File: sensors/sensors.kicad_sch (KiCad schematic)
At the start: 5 parts, among them J1 GPIO, J3 JP_PWM, J4 JP_ADC

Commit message: move buzzer to power board
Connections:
- no-connect marks 14 -> 15
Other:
- removed sheet Buzzer
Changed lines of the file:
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@@
 	)
 	(no_connect
+		(at 73.66 74.93)
+	)
+	(no_connect
 		(at 60.96 82.55)
 	)
@@
 	(wire
 		(pts
-			(xy 294.64 189.23) (xy 297.18 189.23)
-		)
-		(stroke
-			(width 0)
-			(type default)
-		)
-	)
-	(wire
-		(pts
 			(xy 54.61 214.63) (xy 54.61 212.09)
 		)
@@
 		)
 	)
-	(label "GPIO12{slash}PWM0"
-		(at 297.18 189.23 0)
-		(effects
-			(font
-				(size 1.27 1.27)
-			)
-			(justify left bottom)
-		)
-	)
 	(label "GPIO17"
 		(at 31.75 49.53 0)
@@
 				)
 			)
-		)
-	)
-	(sheet
-		(at 266.7 180.34)
-		(size 27.94 17.78)
-		(exclude_from_sim no)
-		(in_bom yes)
-		(on_board yes)
-		(dnp no)
-		(fields_autoplaced yes)
-		(stroke
-			(width 0.1524)
-			(type solid)
-		)
-		(fill
-			(color 0 0 0 0)
-		)
-		(property "Sheetname" "Buzzer"
-			(at 266.7 179.6284 0)
-			(show_name no)
-			(do_not_autoplace no)
-			(effects
-				(font
-					(size 1.27 1.27)
-				)
-				(justify left bottom)
-			)
-		)
-		(property "Sheetfile" "_buzzer.kicad_sch"
-			(at 266.7 198.7046 0)
-			(show_name no)
-			(do_not_autoplace no)
-			(effects
-				(font
-					(size 1.27 1.27)
-				)
-				(justify left top)
-			)
-		)
-		(pin "PWM" input
-			(at 294.64 189.23 0)
-			(effects
-				(font
-					(size 1.27 1.27)
-				)
-				(justify right)
-			)
-		)
-		(instances
-			(project "sensors"
-				(path "/e63e39d7-6ac0-4ffd-8aa3-1841a4541b55"
-					(page "10")
-				)
-			)

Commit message: add Vref
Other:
- added sheet Vref (_vref.kicad_sch)
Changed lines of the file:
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@@
+	)
+	(sheet
+		(at 62.23 239.395)
+		(size 27.94 17.145)
+		(exclude_from_sim no)
+		(in_bom yes)
+		(on_board yes)
+		(dnp no)
+		(fields_autoplaced yes)
+		(stroke
+			(width 0.1524)
+			(type solid)
+		)
+		(fill
+			(color 0 0 0 0)
+		)
+		(property "Sheetname" "Vref"
+			(at 62.23 238.6834 0)
+			(show_name no)
+			(do_not_autoplace no)
+			(effects
+				(font
+					(size 1.27 1.27)
+				)
+				(justify left bottom)
+			)
+		)
+		(property "Sheetfile" "_vref.kicad_sch"
+			(at 62.23 257.1246 0)
+			(show_name no)
+			(do_not_autoplace no)
+			(effects
+				(font
+					(size 1.27 1.27)
+				)
+				(justify left top)
+			)
+		)
+		(instances
+			(project "sensors"
+				(path "/e63e39d7-6ac0-4ffd-8aa3-1841a4541b55"
+					(page "10")
+				)
+			)
+		)
 	)
 	(sheet

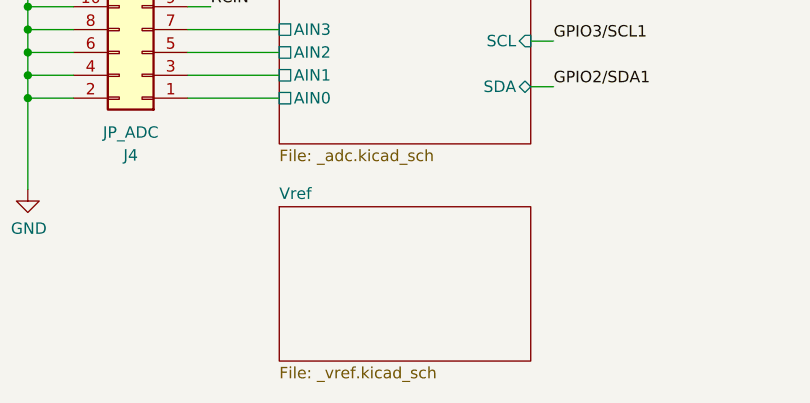
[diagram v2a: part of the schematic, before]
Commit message: remove Vref
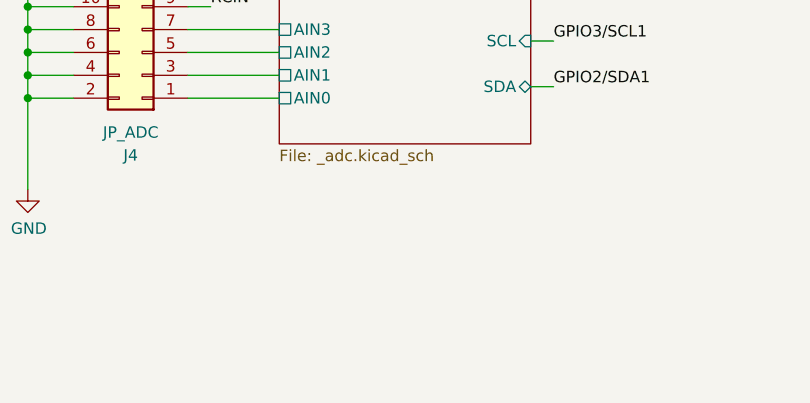
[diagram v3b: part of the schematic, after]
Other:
- removed sheet Vref
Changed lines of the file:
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@@
-	)
-	(sheet
-		(at 62.23 239.395)
-		(size 27.94 17.145)
-		(exclude_from_sim no)
-		(in_bom yes)
-		(on_board yes)
-		(dnp no)
-		(fields_autoplaced yes)
-		(stroke
-			(width 0.1524)
-			(type solid)
-		)
-		(fill
-			(color 0 0 0 0)
-		)
-		(property "Sheetname" "Vref"
-			(at 62.23 238.6834 0)
-			(show_name no)
-			(do_not_autoplace no)
-			(effects
-				(font
-					(size 1.27 1.27)
-				)
-				(justify left bottom)
-			)
-		)
-		(property "Sheetfile" "_vref.kicad_sch"
-			(at 62.23 257.1246 0)
-			(show_name no)
-			(do_not_autoplace no)
-			(effects
-				(font
-					(size 1.27 1.27)
-				)
-				(justify left top)
-			)
-		)
-		(instances
-			(project "sensors"
-				(path "/e63e39d7-6ac0-4ffd-8aa3-1841a4541b55"
-					(page "10")
-				)
-			)
-		)
 	)
 	(sheet

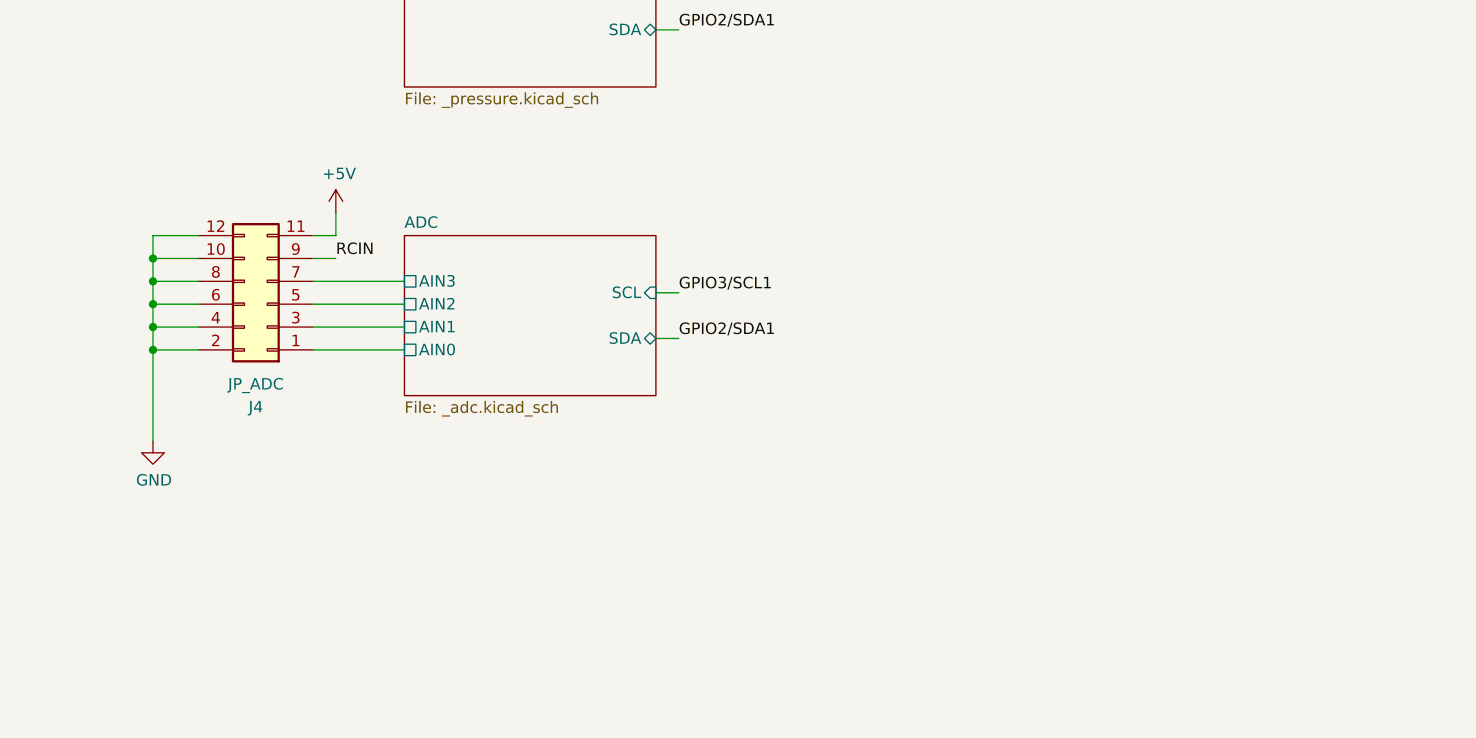
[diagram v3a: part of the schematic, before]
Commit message: added JP_VOLTS, Vref select jumper; VBAT_ADC Jumper
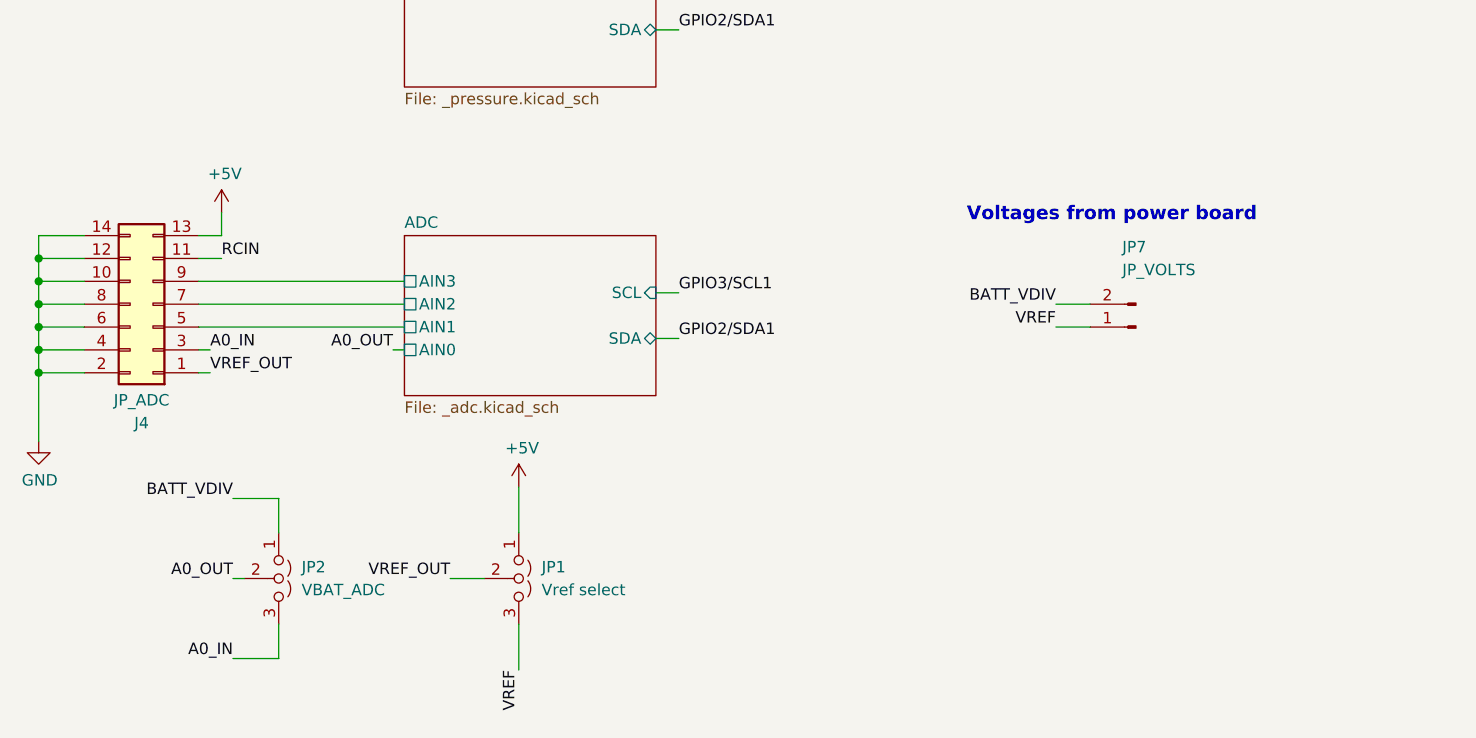
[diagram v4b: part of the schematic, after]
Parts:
- added JP1: Vref select, Connector_PinHeader_2.54mm:PinHeader_1x03_P2.54mm_Vertical, symbol Jumper:Jumper_3_Open
- added JP2: VBAT_ADC, Connector_PinHeader_2.54mm:PinHeader_1x03_P2.54mm_Vertical, symbol Jumper:Jumper_3_Open
- added JP7: JP_VOLTS, Connector_PinHeader_2.54mm:PinHeader_1x02_P2.54mm_Vertical, symbol Connector:Conn_01x02_Pin
- J4: footprint Connector_PinHeader_2.54mm:PinHeader_2x06_P2.54mm_Horizontal -> Connector_PinHeader_2.54mm:PinHeader_2x07_P2.54mm_Horizontal; symbol Connector_Generic:Conn_02x06_Odd_Even -> Connector_Generic:Conn_02x07_Odd_Even
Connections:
- net +5V: now also J4.13 (Pin_13), JP1.1 (A); no longer J4.11 (Pin_11)
- net ADC/AIN1: now also J4.5 (Pin_5); no longer J4.3 (Pin_3)
- net ADC/AIN2: now also J4.7 (Pin_7); no longer J4.5 (Pin_5)
- net ADC/AIN3: now also J4.9 (Pin_9); no longer J4.7 (Pin_7)
- net GND: now also J4.14 (Pin_14)
- net RCIN: now also J4.11 (Pin_11); no longer J4.9 (Pin_9)
- net ADC/AIN0 renamed VREF_OUT
- net VREF_OUT: now also JP1.2 (C)
- new net A0_IN: J4.3 (Pin_3), JP2.3 (B)
- new net A0_OUT: JP2.2 (C)
- new net BATT_VDIV: JP2.1 (A), JP7.2 (Pin_2)
- new net VREF: JP1.3 (B), JP7.1 (Pin_1)
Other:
- note added: "Voltages from power board"

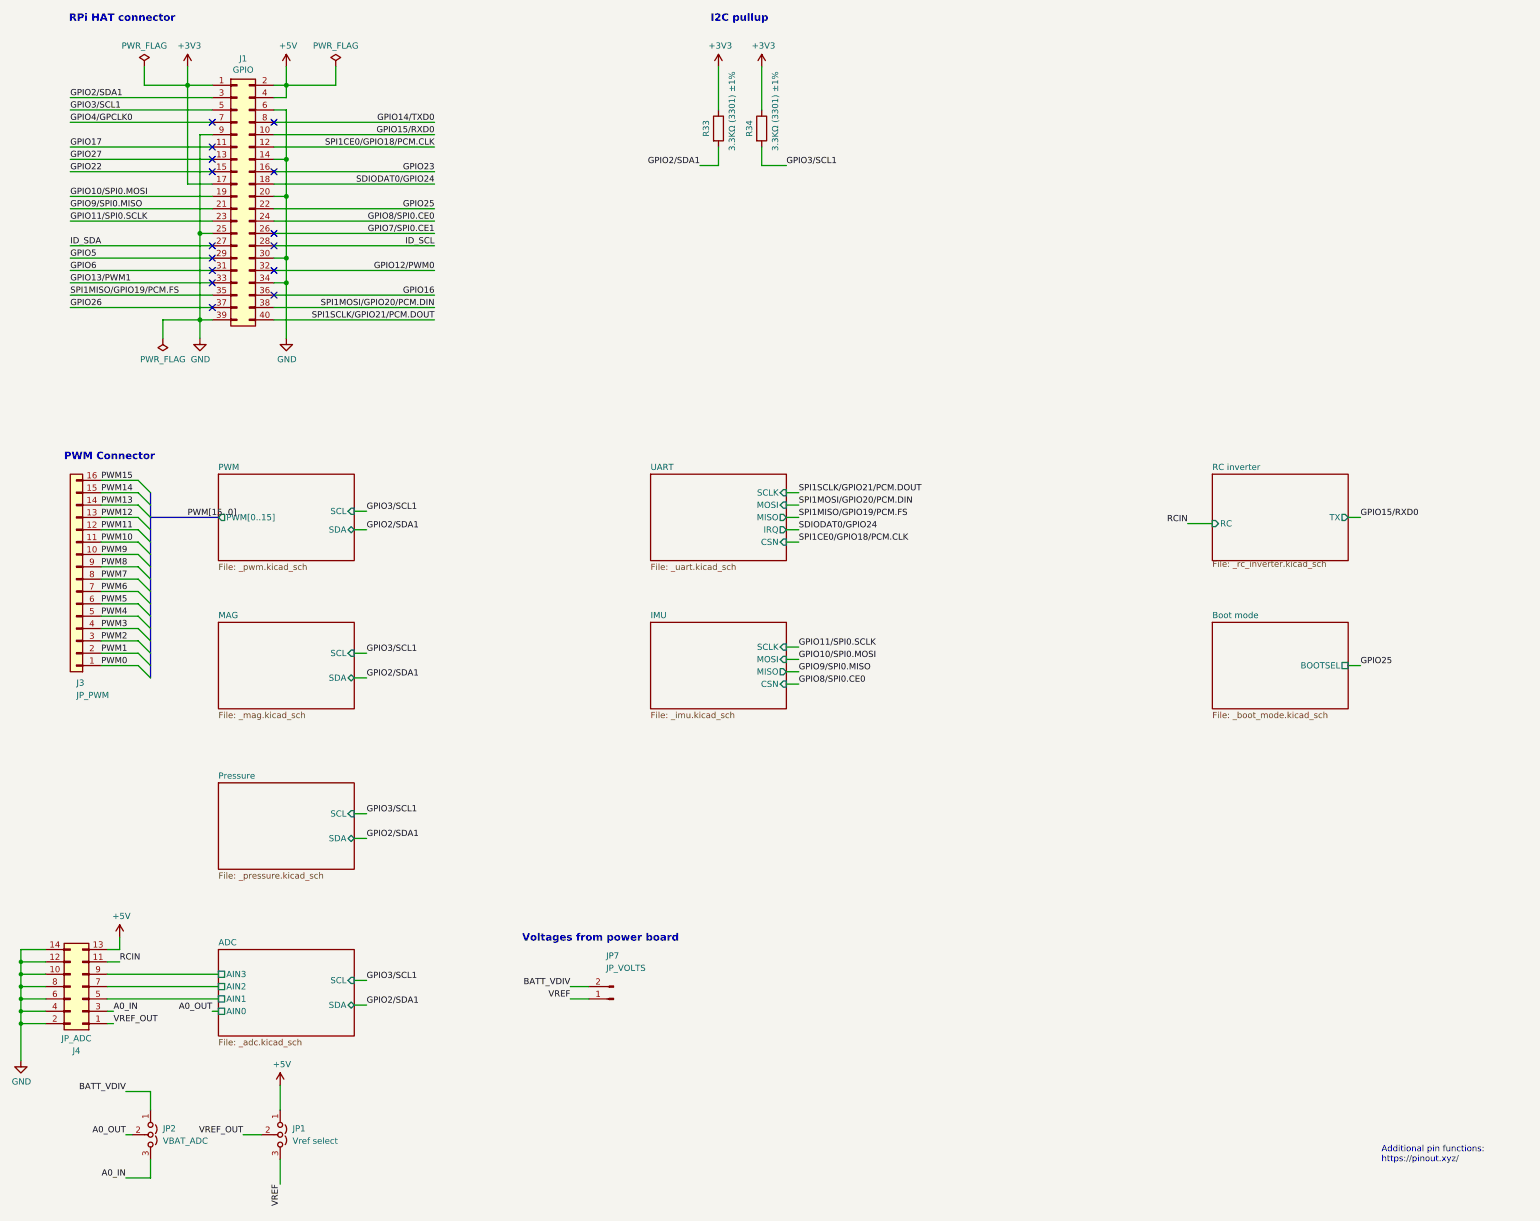
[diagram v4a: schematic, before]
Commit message: add CAN IF
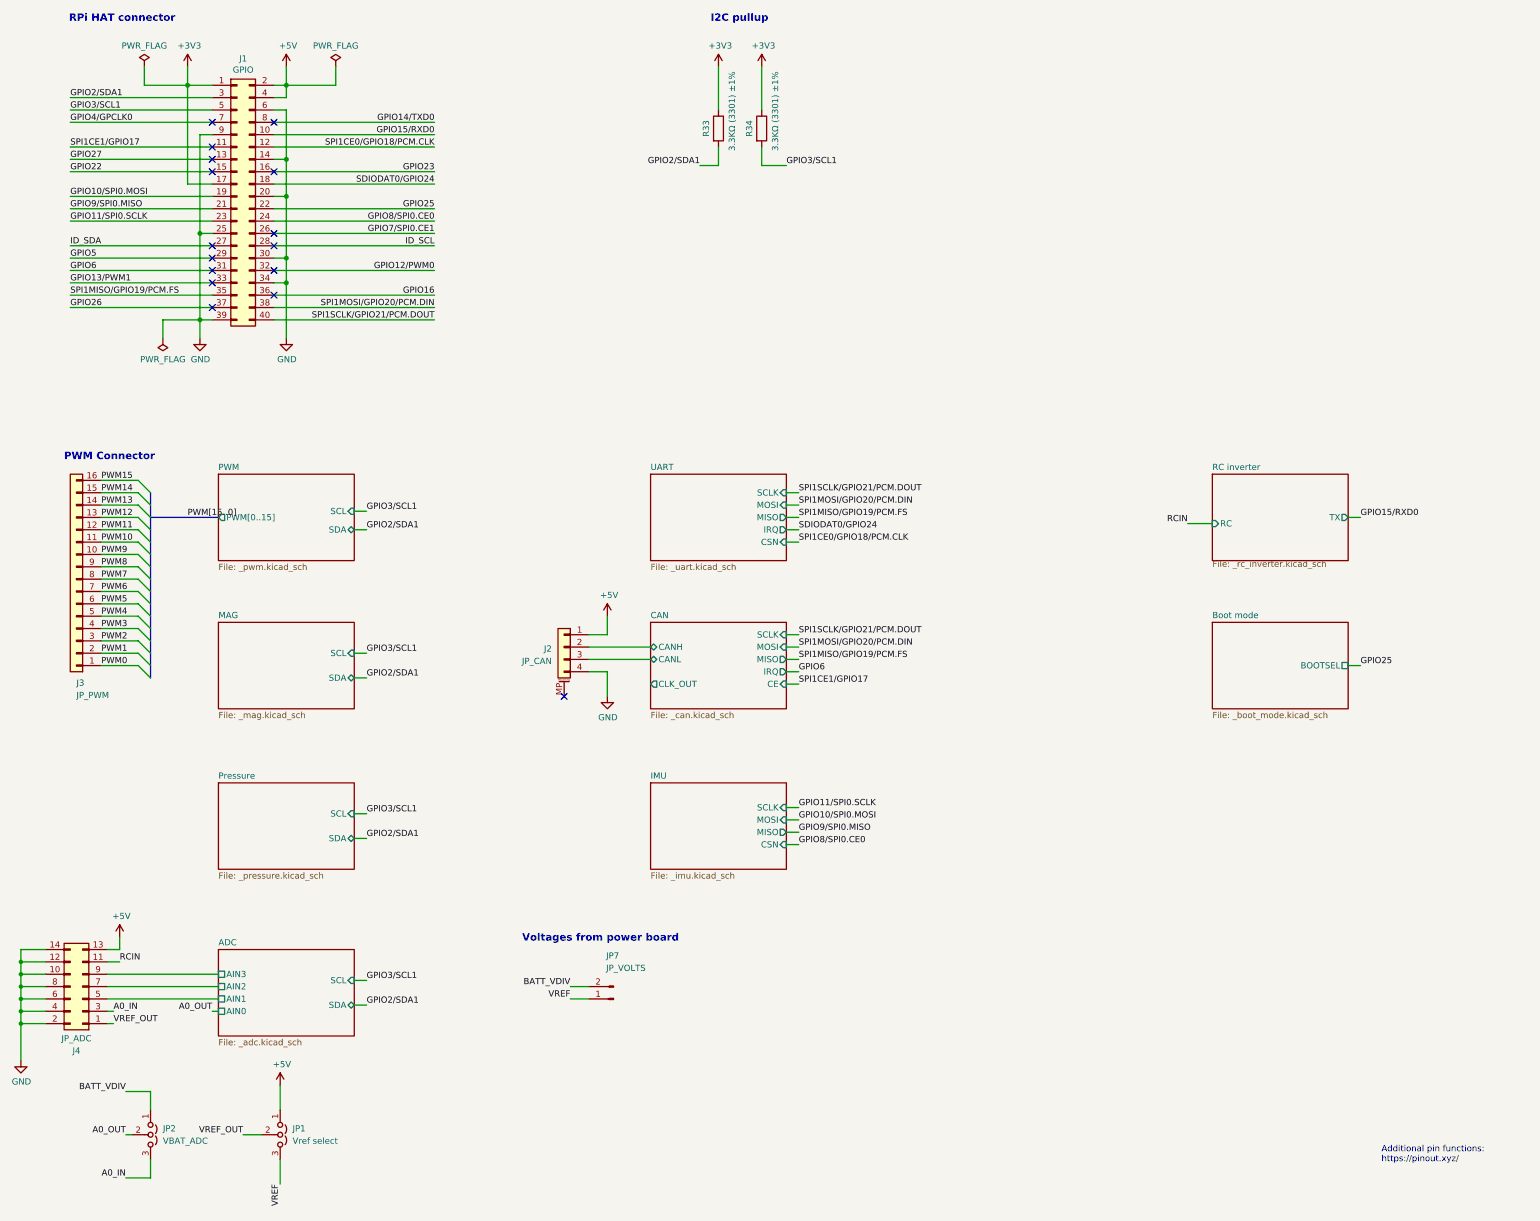
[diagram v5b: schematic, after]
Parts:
- added J2: JP_CAN, Connector_JST:JST_GH_BM04B-GHS-TBT_1x04-1MP_P1.25mm_Vertical, symbol Connector_Generic_MountingPin:Conn_01x04_MountingPin
- JP1, JP2: Part (none) -> 2541WV-3X01P
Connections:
- net +5V: now also J2.1 (Pin_1)
- net GND: now also J2.4 (Pin_4)
- net GPIO17 renamed SPI1CE1/GPIO17
- new net CAN/CANH: J2.2 (Pin_2)
- new net CAN/CANL: J2.3 (Pin_3)
- no-connect marks 15 -> 16
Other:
- added sheet CAN (_can.kicad_sch)
